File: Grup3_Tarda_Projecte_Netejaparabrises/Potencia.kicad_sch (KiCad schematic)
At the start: 47 parts, among them J8 CONNECTOR ALIMENTACIO 01x10, K1 1393280-6, K2 1393280-6, K3 1393280-6, K4 1393280-6, K5 1393280-6, K6 1393280-6, K7 1393280-6, K8 1393280-6, K9 1393280-6, Q1 BC817-25_RF, Q2 BC817-25_RF, Q3 BC817-25_RF, Q4 BC817-25_RF, Q5 BC817-25_RF, Q6 BC817-25_RF, Q7 BC817-25_RF

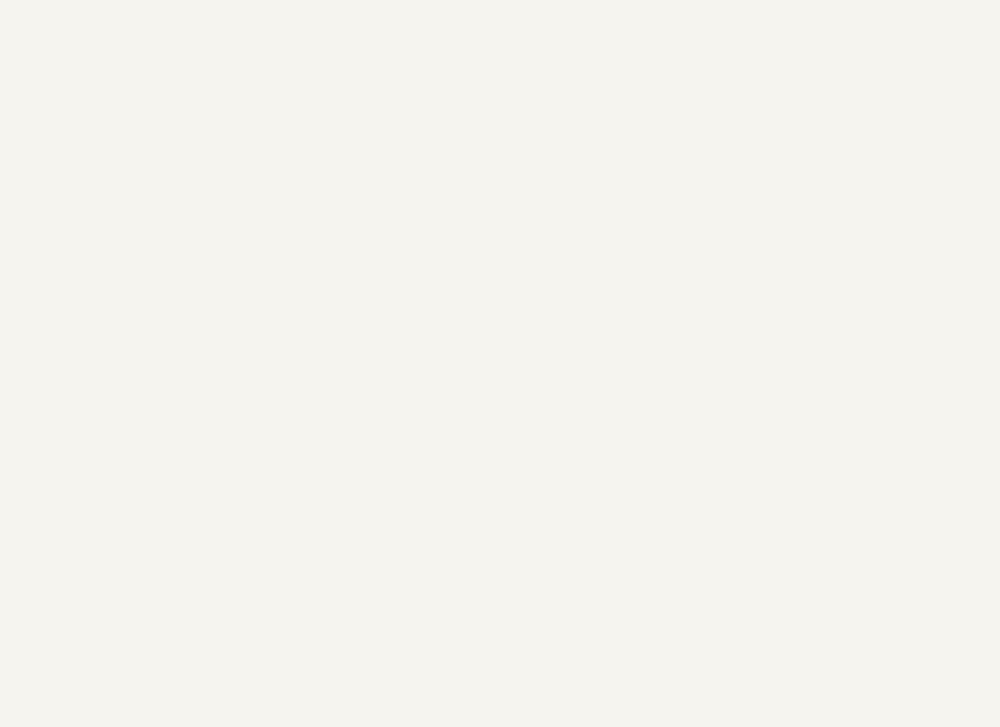
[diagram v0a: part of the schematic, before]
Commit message: canvis reles
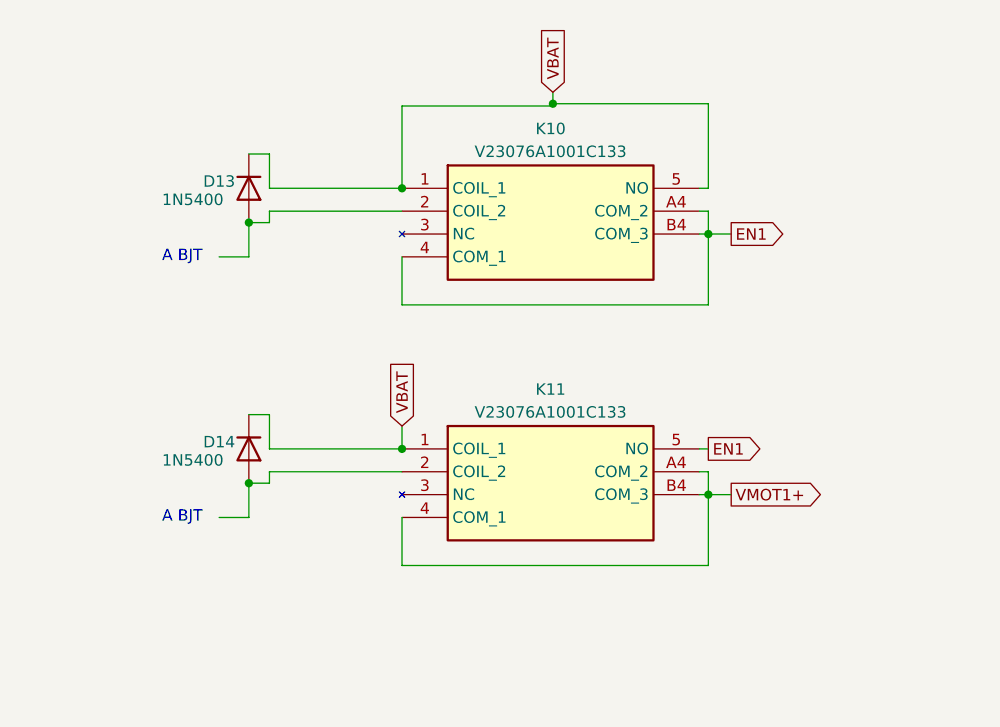
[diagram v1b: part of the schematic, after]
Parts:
- added D13, D14: 1N5400, Diode_THT:D_DO-201AD_P15.24mm_Horizontal, symbol Diode:1N5400
- added K10, K11: V23076A1001C133, V23076A1001C133, symbol V23076A1001C133:V23076A1001C133
- K1, K2, K3, K4, K5, K6, K7, K8, K9: footprint V23076A1001C133:V23076A1001C133 -> Projecte:V23076A1001C133
- Q1, Q2, Q3, Q4, Q5, Q6, Q7: footprint BC817-25_RF:SOT95P237X112-3N -> Projecte:SOT95P237X112-3N
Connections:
- net EN1: now also K10.4 (COM_1), K10.A4 (COM_2), K10.B4 (COM_3), K11.5 (NO)
- net VBAT: now also D13.1 (K), D14.1 (K), K10.1 (COIL_1), K10.5 (NO), K11.1 (COIL_1)
- net VMOT1+: now also K11.4 (COM_1), K11.A4 (COM_2), K11.B4 (COM_3)
- new net: D13.2 (A), K10.2 (COIL_2)
- new net: D14.2 (A), K11.2 (COIL_2)
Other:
- note added: "A BJT"

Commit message: Layout 3
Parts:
- removed D13, D14: 1N5400, Diode_THT:D_DO-201AD_P15.24mm_Horizontal, symbol Diode:1N5400
- removed K10, K11: V23076A1001C133, V23076A1001C133, symbol V23076A1001C133:V23076A1001C133
- K1, K2, K3, K4, K5, K6, K7, K8, K9: footprint Projecte:V23076A1001C133 -> V23076A1001C133:V23076A1001C133
- Q1, Q2, Q3, Q4, Q5, Q6, Q7: footprint Projecte:SOT95P237X112-3N -> BC817-25_RF:SOT95P237X112-3N
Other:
- note removed: "A BJT"
- note removed: "Els senyals EnableM1 i EnableM2 fan la funcio de habilitar els senyals DriverM1 i DriverM2 respectivament. Mentre els senyals d'habilitacio estiguin apagats, els senyals que posen en en funcionament el motor no tindran cap efecte. Un cop activats els senyals enable, els motors es podran fer servir"

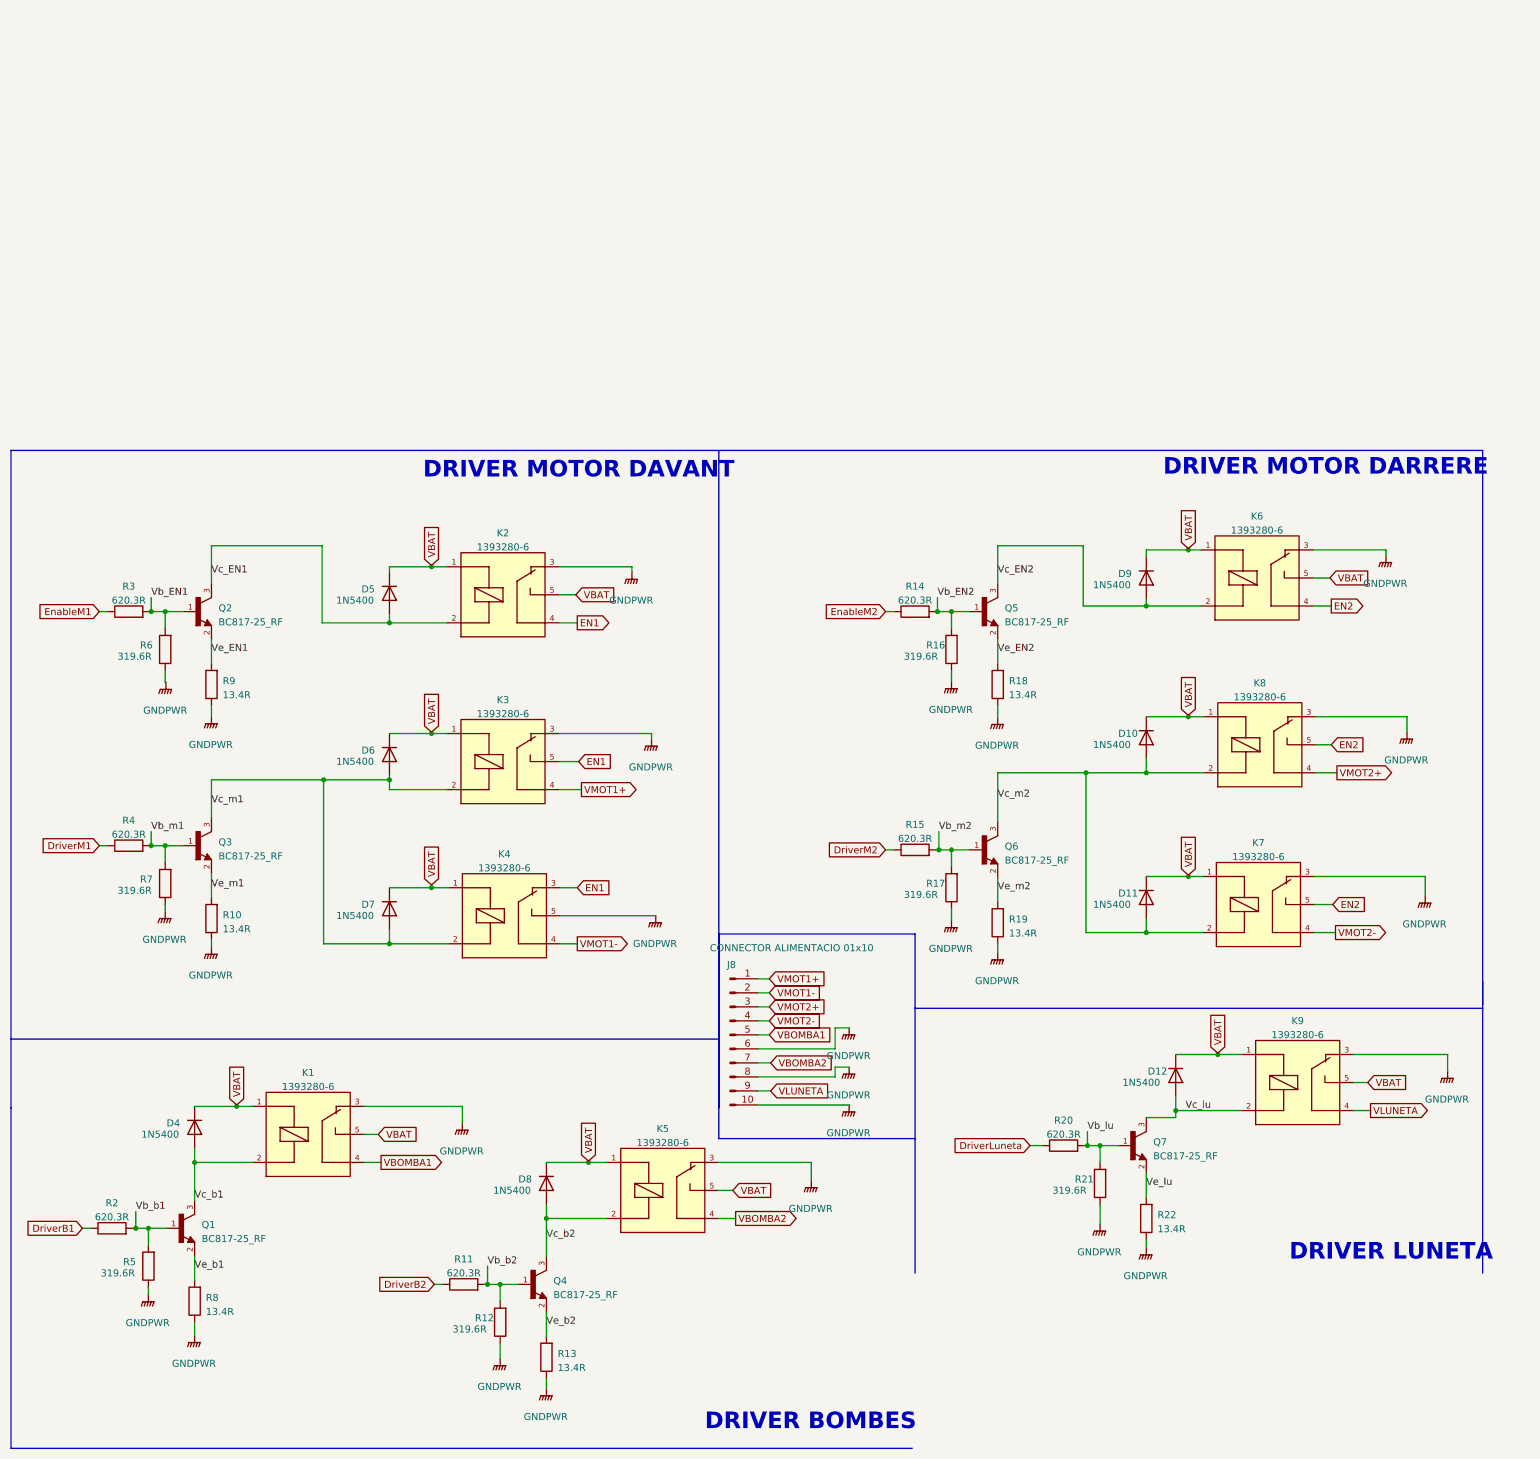
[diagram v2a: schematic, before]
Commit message: canvis menors a esquematic i README
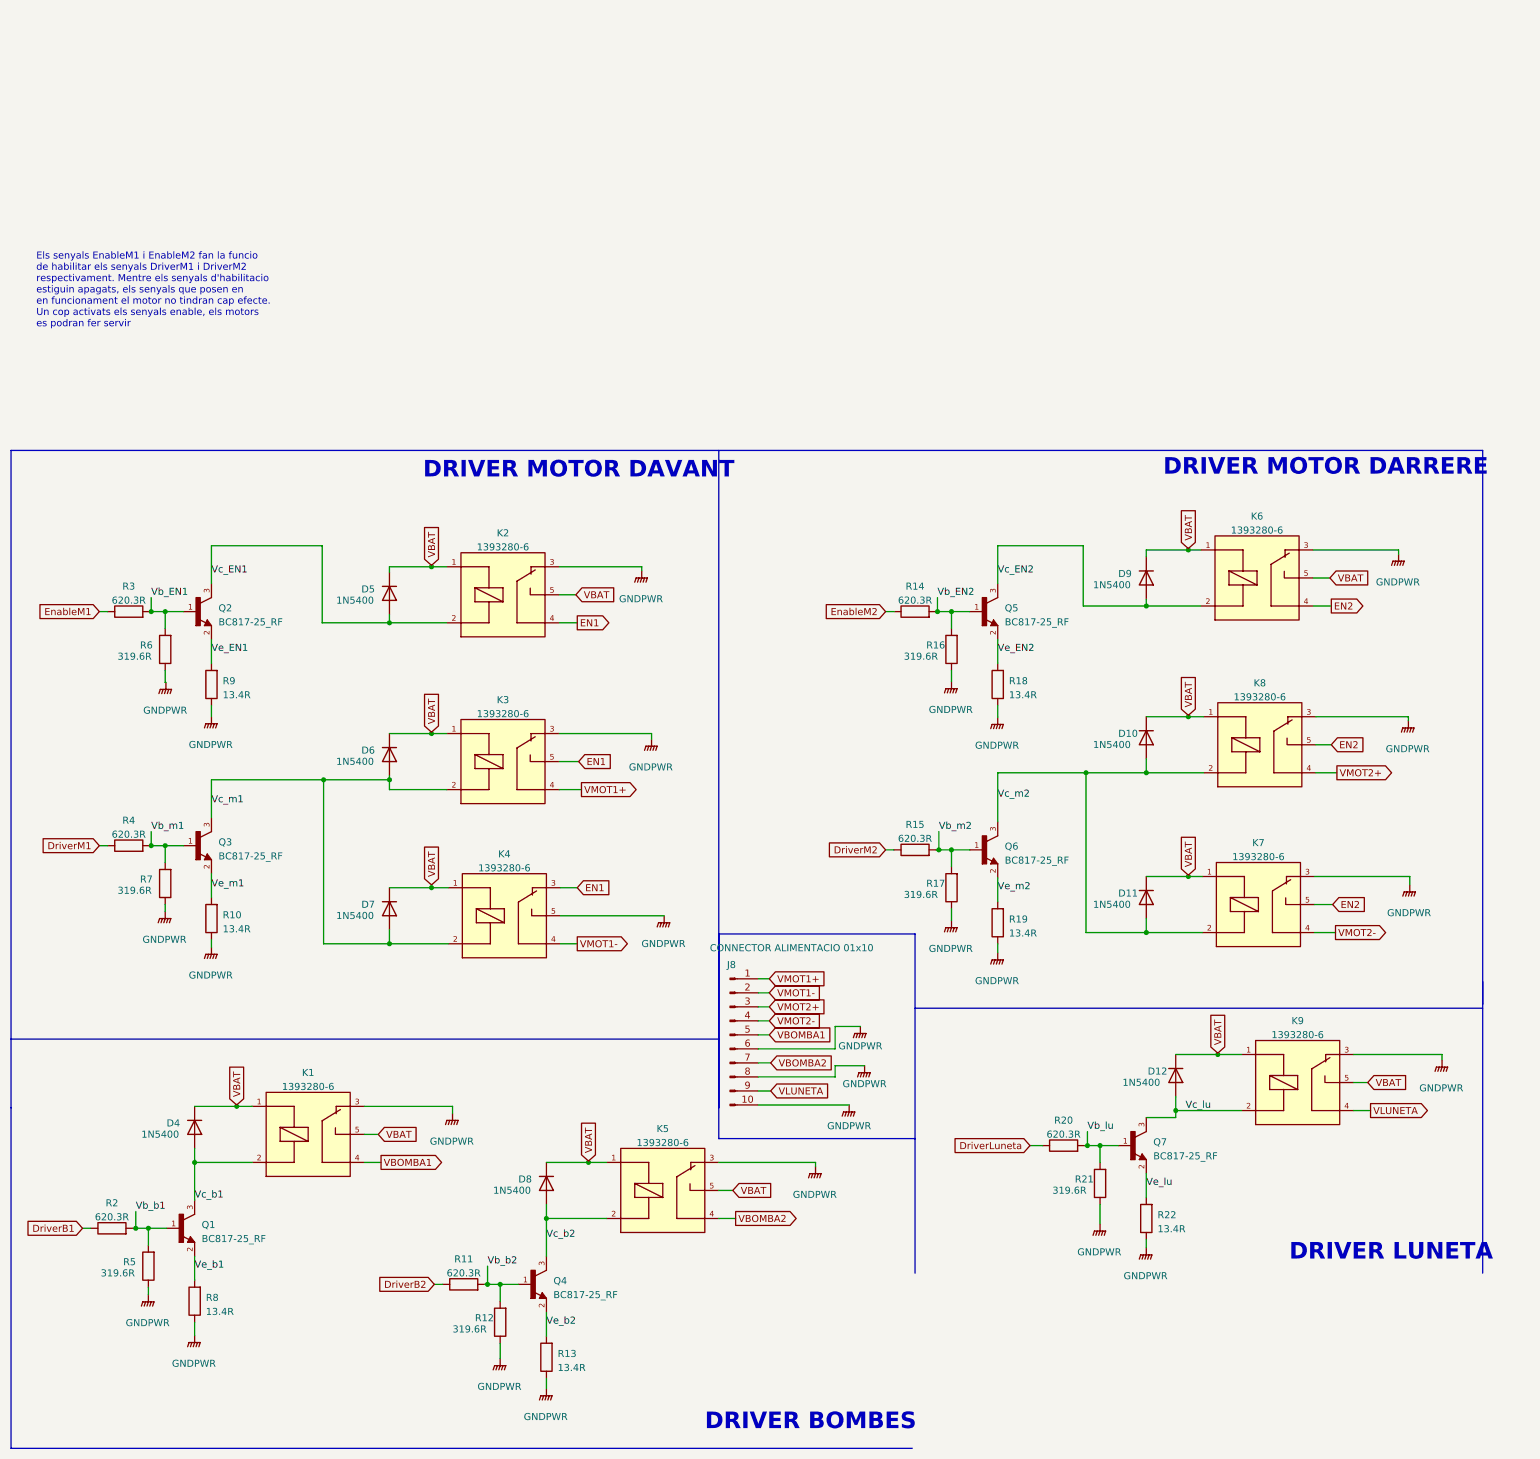
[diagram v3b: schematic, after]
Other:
- note added: "Els senyals EnableM1 i EnableM2 fan la funcio de habilitar els senyals DriverM1 i DriverM2 respectivament. Mentre els senyals d'habilitacio estiguin apagats, els senyals que posen en en funcionament el motor no tindran cap efecte. Un cop activats els senyals enable, els motors es podran fer servir"
